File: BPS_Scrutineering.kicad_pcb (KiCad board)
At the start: 2 copper layers, 87.9 x 87.4 mm, 22 parts, among them J1 Conn_01x01_Female, J10 Conn_01x01_Female, J11 Conn_01x01_Female, J12 Conn_01x01_Female, J13 Conn_01x01_Female, J14 Conn_01x01_Female, J2 Conn_01x01_Female, J3 Conn_01x01_Female, J4 Conn_01x01_Female, J5 Conn_01x01_Female, J6 Conn_01x01_Female, J7 Conn_01x01_Female, J8 Conn_01x01_Female, J9 Conn_01x01_Female, SW1 SW_DIP_x07, SW2 SW_DIP_x07

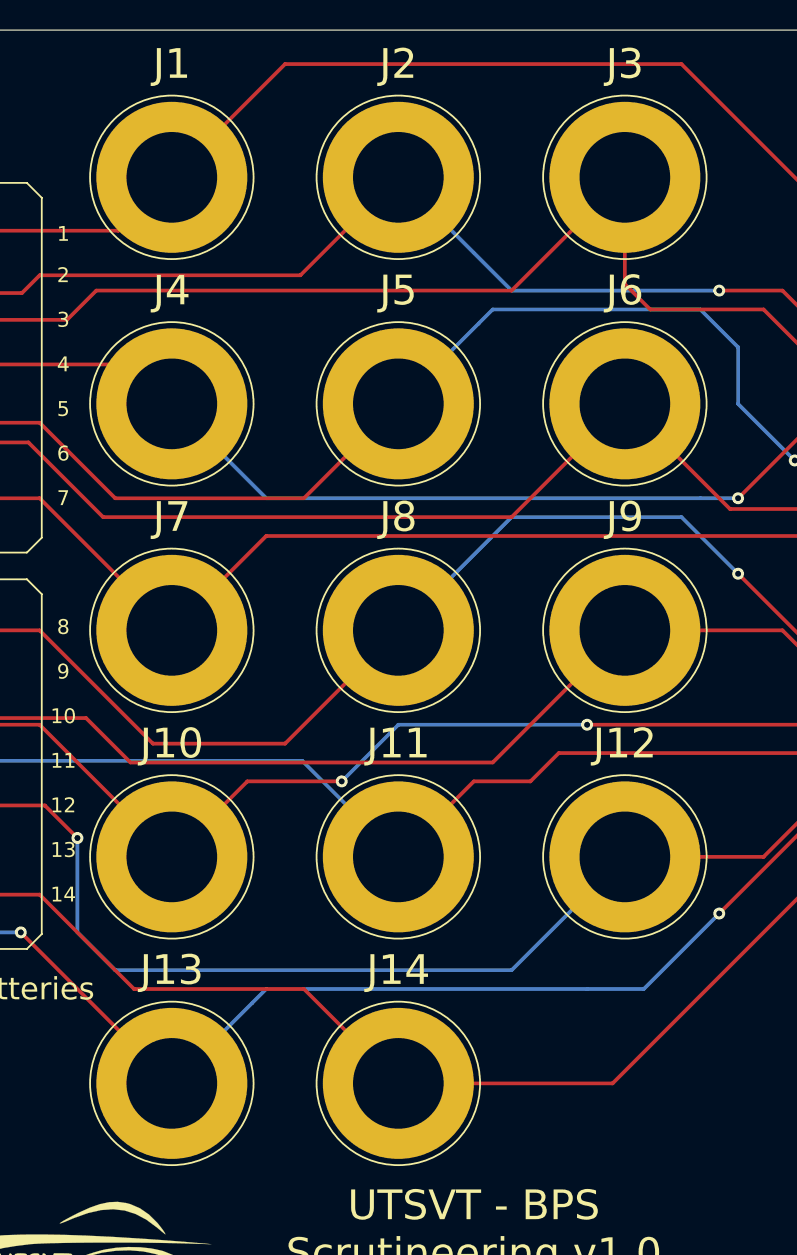
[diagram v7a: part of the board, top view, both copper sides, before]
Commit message: Changed footprints
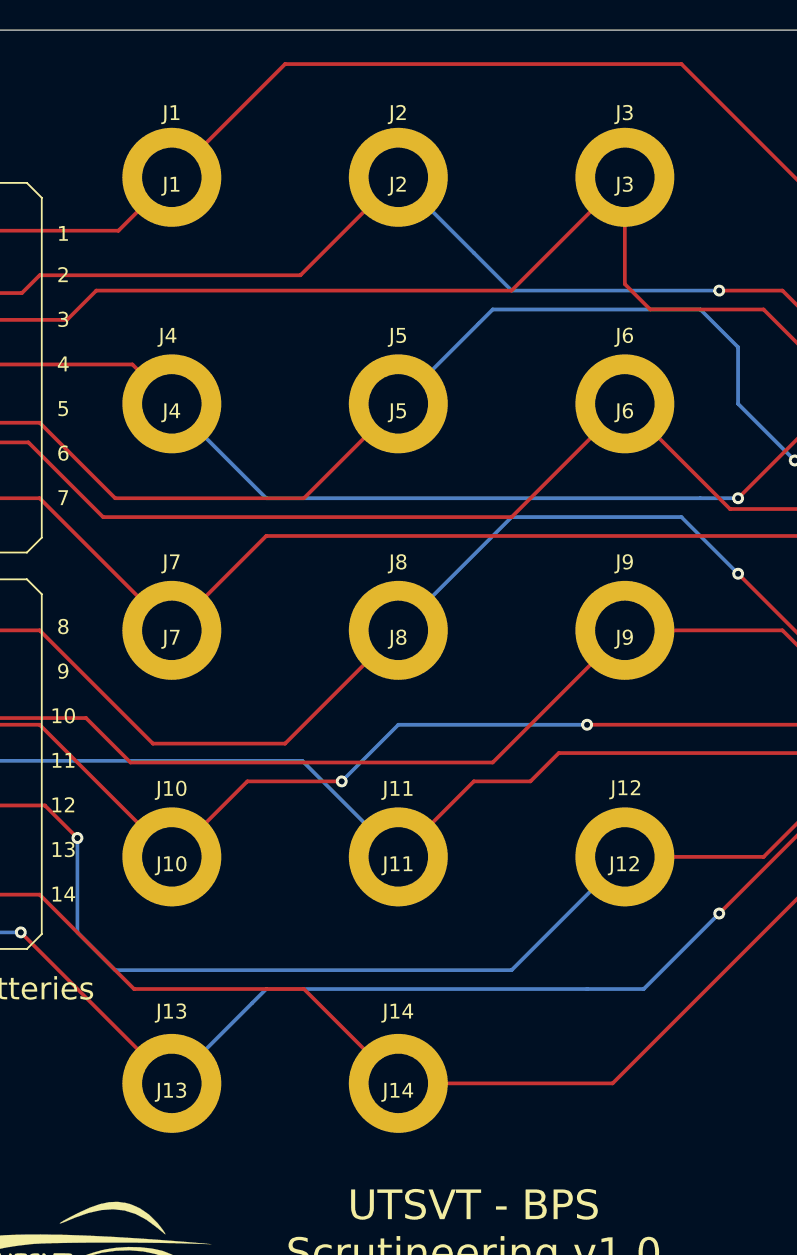
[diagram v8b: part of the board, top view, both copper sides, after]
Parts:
- J1, J10, J11, J12, J13, J14, J2, J3, J4, J5, J6, J7, J8, J9: footprint Connector:Banana_Jack_1Pin -> UTSVT_Connectors:Banana_Jack_1_Pin_4mm
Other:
- board text added: "J1"
- board text added: "J10"
- board text added: "J11"
- board text added: "J12"
- board text added: "J13"
- board text added: "J14"
- board text added: "J2"
- board text added: "J3"
- board text added: "J4"
- board text added: "J5"
- board text added: "J6"
- board text added: "J7"
- board text added: "J8"
- board text added: "J9"
